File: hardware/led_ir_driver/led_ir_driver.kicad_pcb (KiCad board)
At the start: 2 copper layers, 70 x 55 mm, 25 parts, among them J1 MCP4725 IR 0x60, J2 PI I2C INPUT / IR OUT, J3 MCP4725 RED 0x61, J5 IR LED A / K, J6 RED LED A / K, J7 5V INPUT / GND, Q1 2N4401 / E-B-C, Q2 2N4401 / E-B-C, U1 LM358P / DIP8 socket

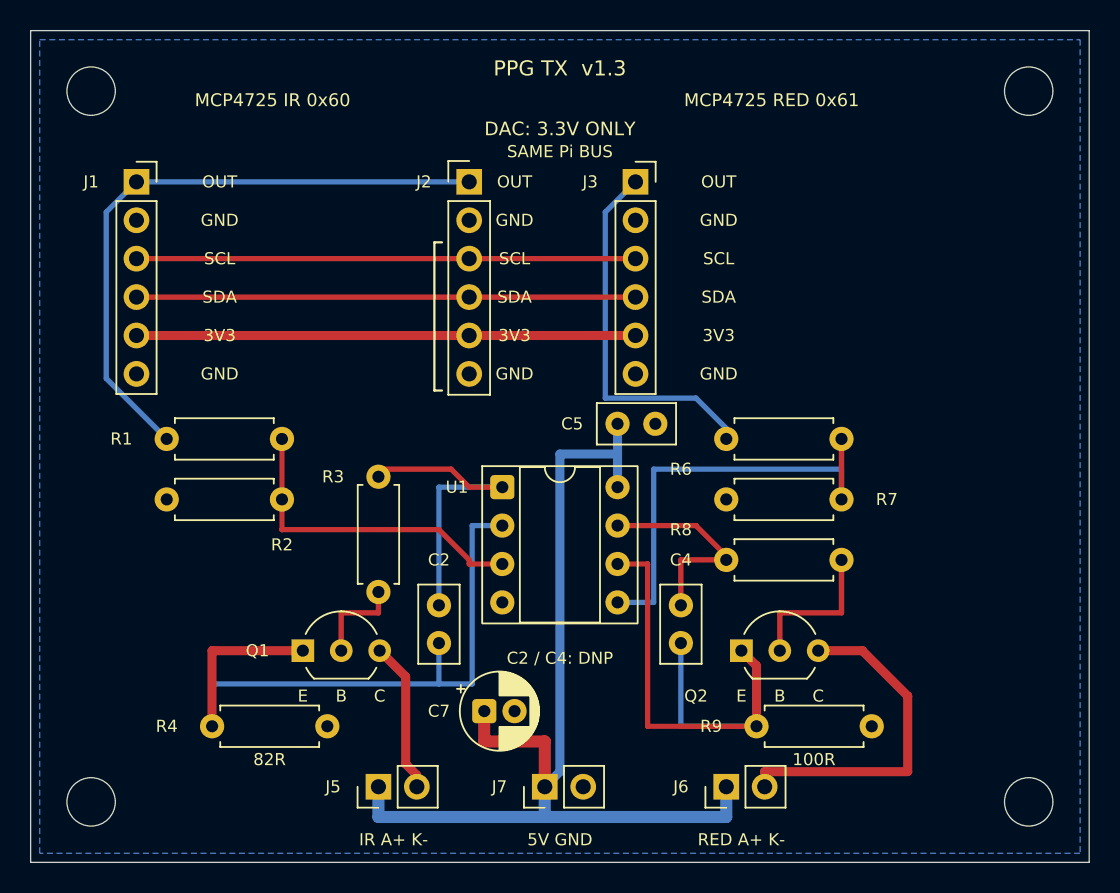
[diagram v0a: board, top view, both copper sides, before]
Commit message: hardware: finalize LED IR driver v1.6 and audit MCP4725 wiring
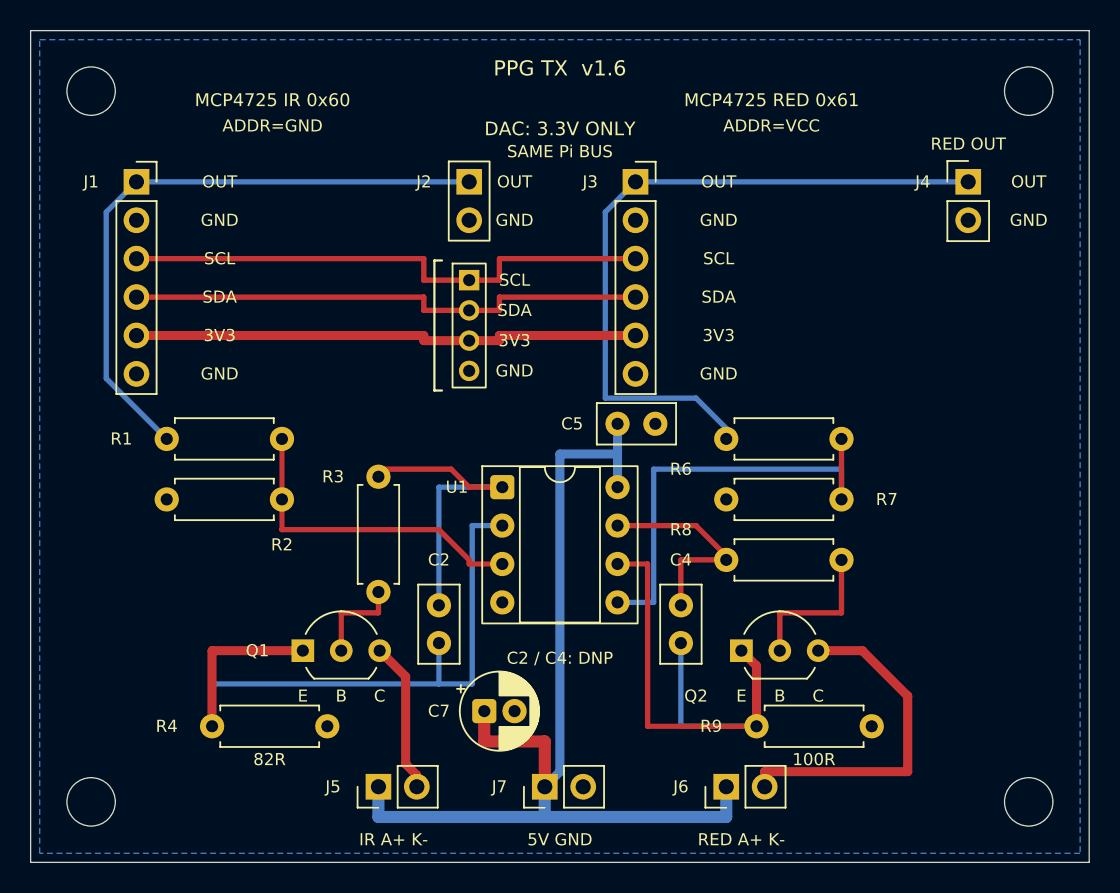
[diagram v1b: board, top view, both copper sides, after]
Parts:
- added J4: RED DAC OUT / GND, TX:Header2, F.Cu at (162.0, 110.0)
- J2: footprint TX:Header6 -> TX:HeaderMixed
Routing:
- net /DAC_RED: track 24.7 -> 46.7 mm
- net /SCL: track 33.0 -> 35.8 mm
- net /SDA: track 33.0 -> 34.8 mm
- net /3V3: track 33.0 -> 33.7 mm
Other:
- board text added: "ADDR=GND"
- board text added: "ADDR=VCC"
- board text added: "J4 RED OUT"
- board text added: "PPG TX v1.6"
- board text added: "RED OUT"
- board text removed: "PPG TX v1.3"

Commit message: hardware: use 100 ohm IR LED sense resistor
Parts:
- R4: value 82R 1% 0.25W -> 100R 1% 0.25W
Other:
- board text removed: "82R"
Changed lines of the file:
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@@
 			)
 		)
-		(property "Value" "82R 1% 0.25W"
+		(property "Value" "100R 1% 0.25W"
 			(at 3.81 2.37 0)
 			(layer "F.Fab")
@@
 		)
 	)
-	(gr_text "82R"
+	(gr_text "100R"
 		(at 115.8 148.2 0)
 		(layer "F.SilkS")

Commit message: Compact PPG boards, add receiver filters and package V-cut panel
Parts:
- moved H1 21.0 mm to (104.0, 125.0)
- moved H2 21.0 mm to (166.0, 125.0)
- moved C2 5.00 mm to (127.0, 133.0)
- moved C4 5.00 mm to (143.0, 133.0)
- moved C5 5.00 mm to (138.8, 121.0)
- moved C7 5.00 mm to (130.0, 140.0)
- moved H3 5.00 mm to (104.0, 146.0)
- moved H4 5.00 mm to (166.0, 146.0)
- moved J1 5.00 mm to (107.0, 105.0)
- moved J2 5.00 mm to (129.0, 105.0)
- moved J3 5.00 mm to (140.0, 105.0)
- moved J4 5.00 mm to (162.0, 105.0)
- moved J5 5.00 mm to (123.0, 145.0)
- moved J6 5.00 mm to (146.0, 145.0)
- moved J7 5.00 mm to (134.0, 145.0)
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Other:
- board size 70 x 55 mm -> 70 x 50 mm
- board text added: "PPG TX v1.7"
- board text removed: "PPG TX v1.6"

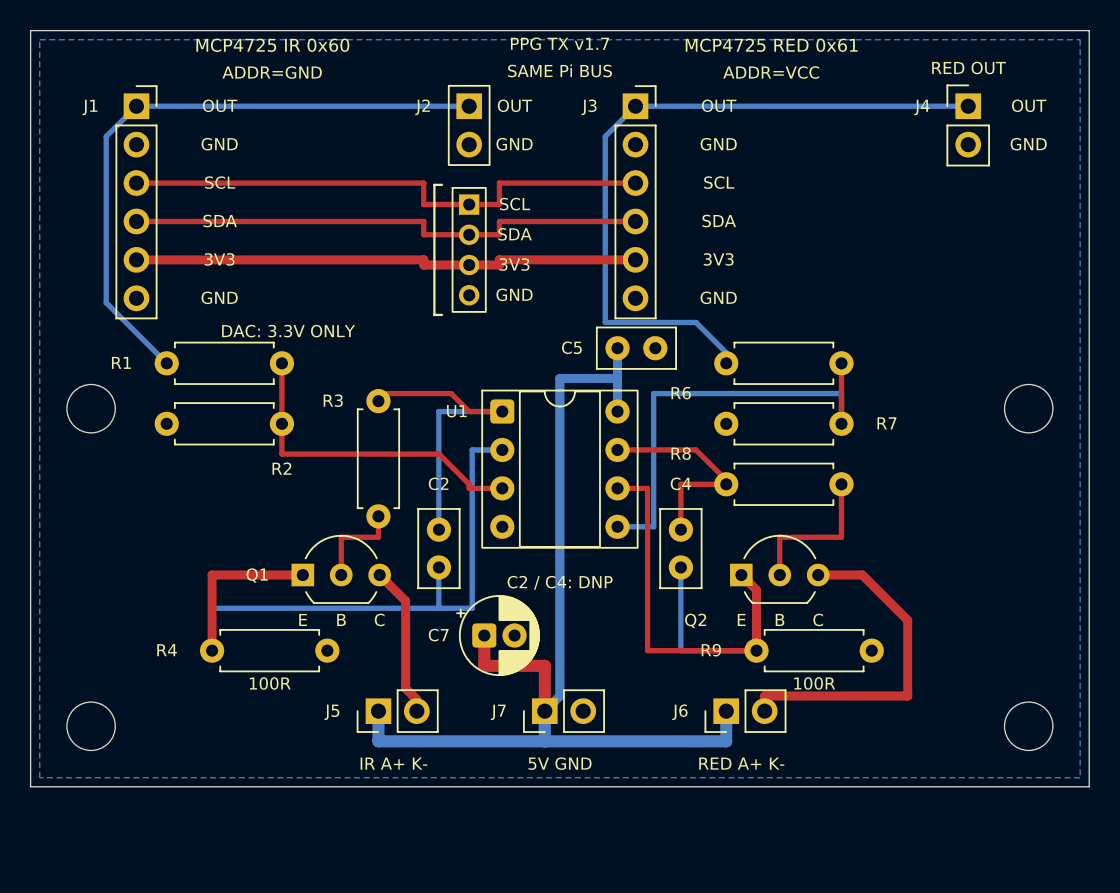
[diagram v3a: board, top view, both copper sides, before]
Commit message: Convert PPG passives to SMD and refresh compact V-cut panel
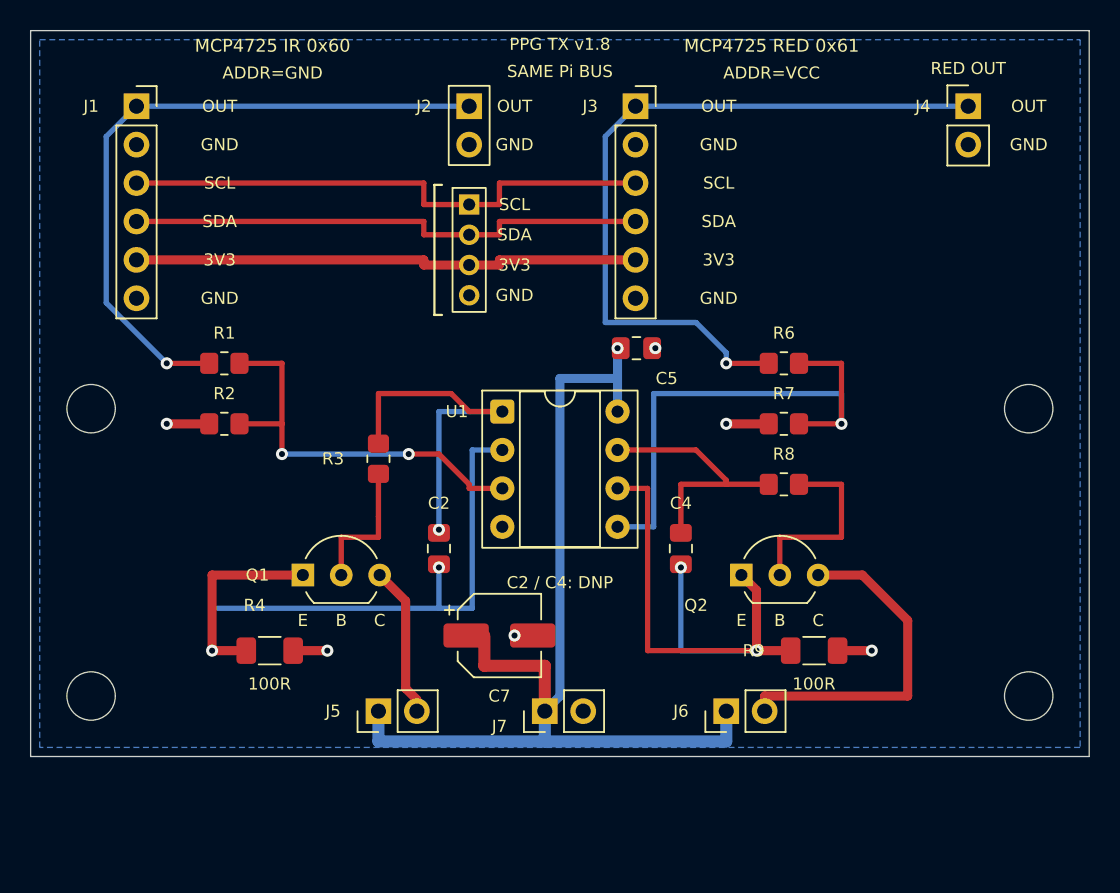
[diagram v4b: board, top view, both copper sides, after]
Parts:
- R4, R9: footprint TX:R -> TX:RSense
- moved R1 3.81 mm to (112.8, 122.0)
- moved R2 3.81 mm to (112.8, 126.0)
- moved R3 3.81 mm to (123.0, 128.3)
- moved R4 3.81 mm to (115.8, 141.0)
- moved R6 3.81 mm to (149.8, 122.0)
- moved R7 3.81 mm to (149.8, 126.0)
- moved R8 3.81 mm to (149.8, 130.0)
- moved R9 3.81 mm to (151.8, 141.0)
- moved H3 2.00 mm to (104.0, 144.0)
- moved H4 2.00 mm to (166.0, 144.0)
- moved C2 1.25 mm to (127.0, 134.2)
- moved C4 1.25 mm to (143.0, 134.2)
- moved C5 1.25 mm to (140.1, 121.0)
- moved C7 1.00 mm to (131.0, 140.0)
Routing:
- net /GND: track 0.00 -> 11.6 mm, vias 0 -> 6
- net /CMD_RED: track 29.6 -> 35.2 mm, vias 0 -> 1
- net /CMD_IR: track 21.7 -> 27.3 mm, vias 0 -> 2
- net /AMP_RED: track 14.3 -> 17.3 mm
- net /AMP_IR: track 21.2 -> 24.2 mm, vias 0 -> 1
- net /DAC_RED: track 46.7 -> 49.5 mm, vias 0 -> 1
- net /BASE_RED: track 10.1 -> 12.9 mm
- net /BASE_IR: track 6.34 -> 9.15 mm
- net /DAC_IR: track 41.5 -> 44.3 mm, vias 0 -> 1
- net /SENSE_IR: track 46.2 -> 48.6 mm, vias 0 -> 2
- net /SENSE_RED: track 35.8 -> 38.3 mm, vias 0 -> 2
- net /5V: track 68.4 -> 69.8 mm, vias 0 -> 1
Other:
- board size 70 x 50 mm -> 70 x 48 mm
- board text added: "PPG TX v1.8"
- board text removed: "5V GND"
- board text removed: "DAC: 3.3V ONLY"
- board text removed: "IR A+ K-"
- board text removed: "J2 PI: SCL SDA 3V3 GND"
- board text removed: "PPG TX v1.7"
- board text removed: "RED A+ K-"

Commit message: Shrink PPG receivers to 70x20 and driver to 70x40; refresh V-cut release
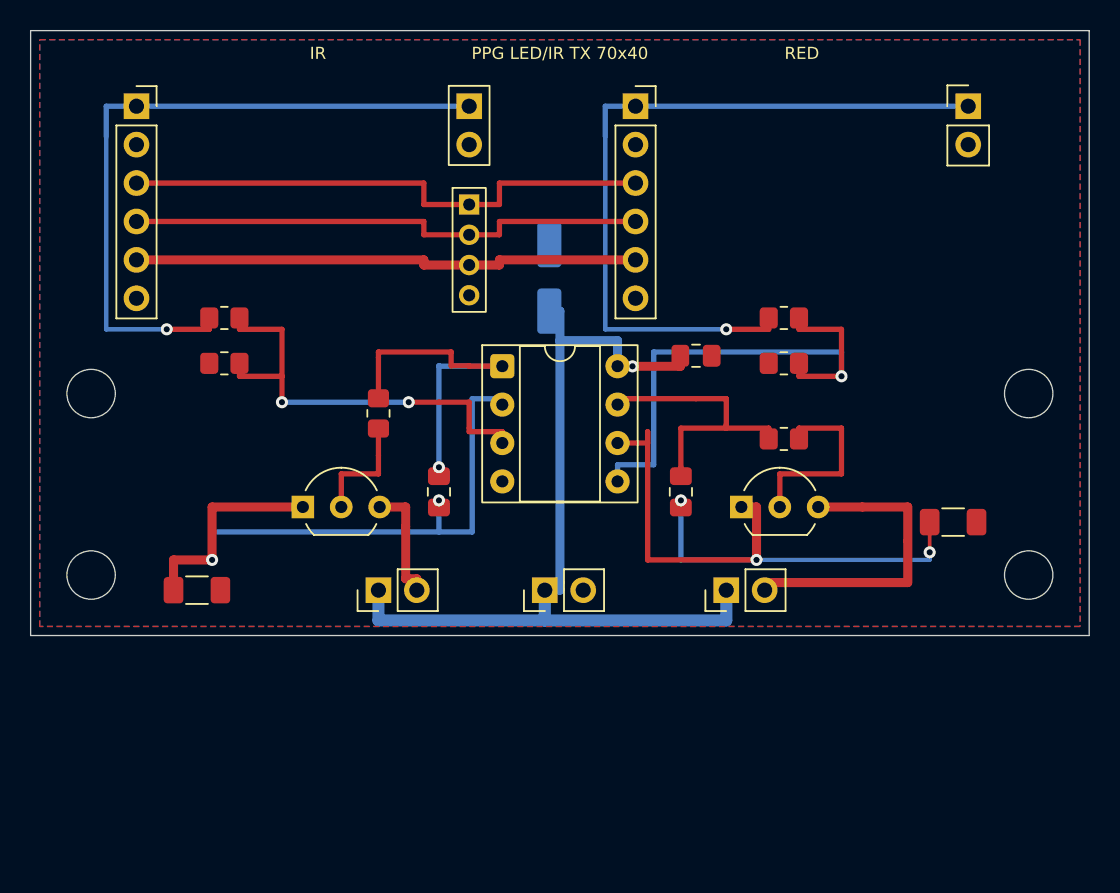
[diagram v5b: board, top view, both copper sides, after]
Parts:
- C7: moved to B.Cu
- moved C7 23.9 mm to (134.3, 116.3), turned to 90 degrees
- moved R9 12.5 mm to (161.0, 132.5)
- moved H3 8.00 mm to (104.0, 136.0)
- moved H4 8.00 mm to (166.0, 136.0)
- moved J5 8.00 mm to (123.0, 137.0)
- moved J6 8.00 mm to (146.0, 137.0)
- moved J7 8.00 mm to (134.0, 137.0)
- moved R4 6.26 mm to (111.0, 137.0)
- moved Q1 4.50 mm to (118.0, 131.5)
- moved Q2 4.50 mm to (147.0, 131.5)
- moved R2 4.00 mm to (112.8, 122.0)
- moved R7 4.00 mm to (149.8, 122.0)
- moved C5 3.97 mm to (144.0, 121.5)
- moved C2 3.75 mm to (127.0, 130.5)
- moved C4 3.75 mm to (143.0, 130.5)
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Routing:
- net /GND: track 11.6 -> 0.00 mm, vias 6 -> 0
- net /5V: track 69.8 -> 59.5 mm
- net /SENSE_RED: track 38.3 -> 46.3 mm, vias 2 -> 3
- net /SENSE_IR: track 48.6 -> 46.5 mm
- net /LED_K_IR: track 10.0 -> 7.96 mm
- net /CMD_IR: track 27.3 -> 29.3 mm
- net /DAC_IR: track 44.3 -> 46.3 mm
- net /LED_K_RED: track 22.6 -> 20.9 mm
- net /AMP_RED: track 17.3 -> 18.8 mm
- net /BASE_IR: track 9.15 -> 7.65 mm
- net /DAC_RED: track 49.5 -> 50.3 mm
- added copper zone on F.Cu, net /GND
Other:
- board size 70 x 48 mm -> 70 x 40 mm
- board text added: "IR"
- board text added: "IR-"
- board text added: "PPG LED/IR TX 70x40"
- board text added: "RED"
- board text added: "RED-"
- board text removed: "100R"
- board text removed: "A+"
- board text removed: "ADDR=GND"
- board text removed: "ADDR=VCC"
- board text removed: "C2 / C4: DNP"
- board text removed: "IR_OUT"
- board text removed: "J1 IR DAC"
- board text removed: "J2 PI"
- board text removed: "J3 RED DAC"
- board text removed: "J4 RED OUT"
- board text removed: "J5 IR LED"
- board text removed: "J6 RED LED"
- board text removed: "J7 POWER"
- board text removed: "K-"
- board text removed: "MCP4725 IR 0x60"
- board text removed: "MCP4725 RED 0x61"
- board text removed: "OUT"
- board text removed: "PPG TX v1.8"
- board text removed: "Q1 IR E-B-C"
- board text removed: "Q2 RED E-B-C"
- board text removed: "RED OUT"
- board text removed: "RED_OUT"
- board text removed: "SAME Pi BUS"
- board text removed: "U1 LM358"

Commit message: Chamfer PPG board routing to 45 degrees and verify V-score fabrication release
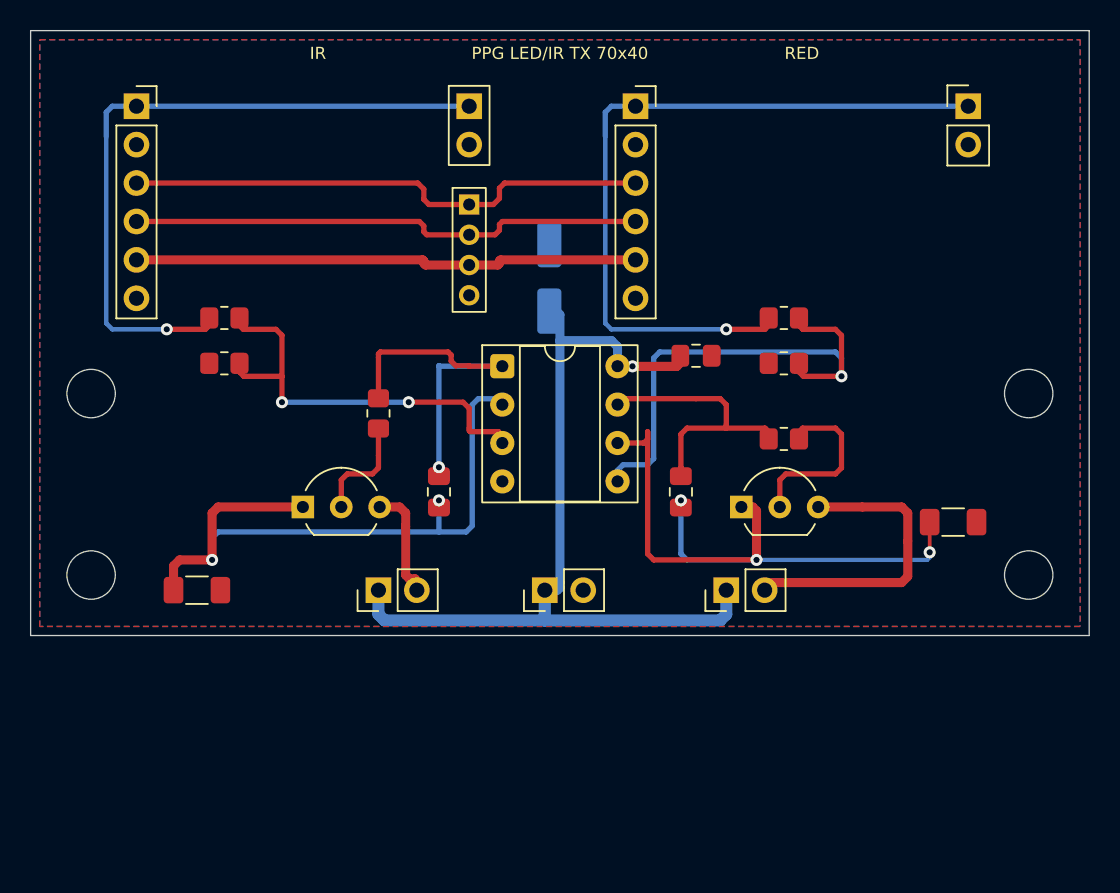
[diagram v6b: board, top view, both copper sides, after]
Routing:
- net /CMD_RED: track 35.3 -> 33.8 mm
- net /SENSE_IR: track 46.5 -> 45.3 mm
- net /5V: track 59.5 -> 58.4 mm
- net /CMD_IR: track 29.3 -> 28.3 mm
- net /SCL: track 35.8 -> 35.0 mm
- net /SENSE_RED: track 46.3 -> 45.4 mm
- net /BASE_RED: track 12.8 -> 12.0 mm
- net /DAC_RED: track 50.3 -> 49.7 mm
- net /DAC_IR: track 46.3 -> 45.7 mm
- net /AMP_RED: track 18.8 -> 18.2 mm
- net /SDA: track 34.8 -> 34.2 mm
- net /LED_K_RED: track 20.9 -> 20.3 mm

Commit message: Lengthen 45-degree PCB bends and refresh fabrication packages
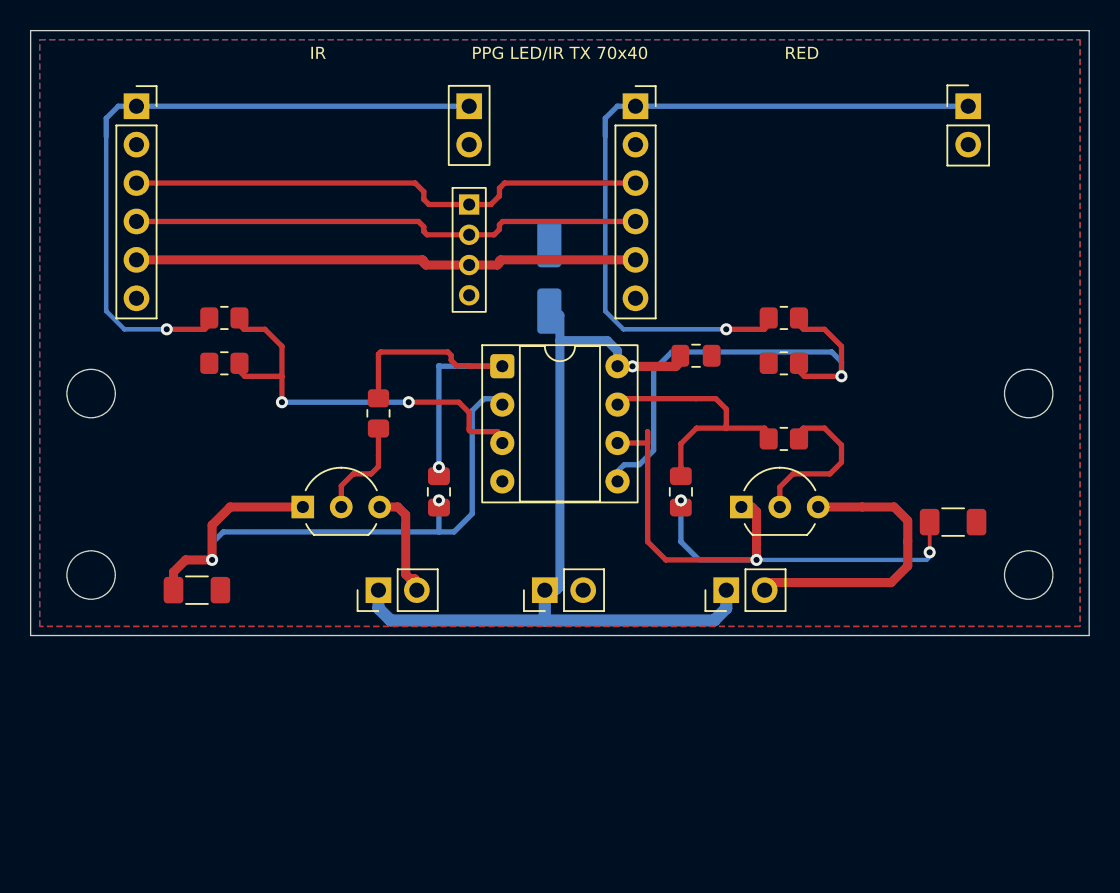
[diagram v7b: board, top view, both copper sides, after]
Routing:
- net /SENSE_IR: track 45.3 -> 43.7 mm
- net /CMD_RED: track 33.8 -> 32.4 mm
- net /BASE_RED: track 12.0 -> 11.0 mm
- net /SENSE_RED: track 45.4 -> 44.6 mm
- net /DAC_RED: track 49.7 -> 49.0 mm
- net /DAC_IR: track 45.7 -> 45.0 mm
- net /LED_K_RED: track 20.3 -> 19.6 mm
- net /5V: track 58.4 -> 57.7 mm
- net /CMD_IR: track 28.3 -> 27.6 mm
- net /AMP_RED: track 18.2 -> 17.7 mm
